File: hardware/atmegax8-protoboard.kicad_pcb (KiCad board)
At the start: 2 copper layers, 22.9 x 55.9 mm, 6 parts, among them IC1 ATMEGA328-P, P1 CONN1, P2 CONN2, P3 SERPROG

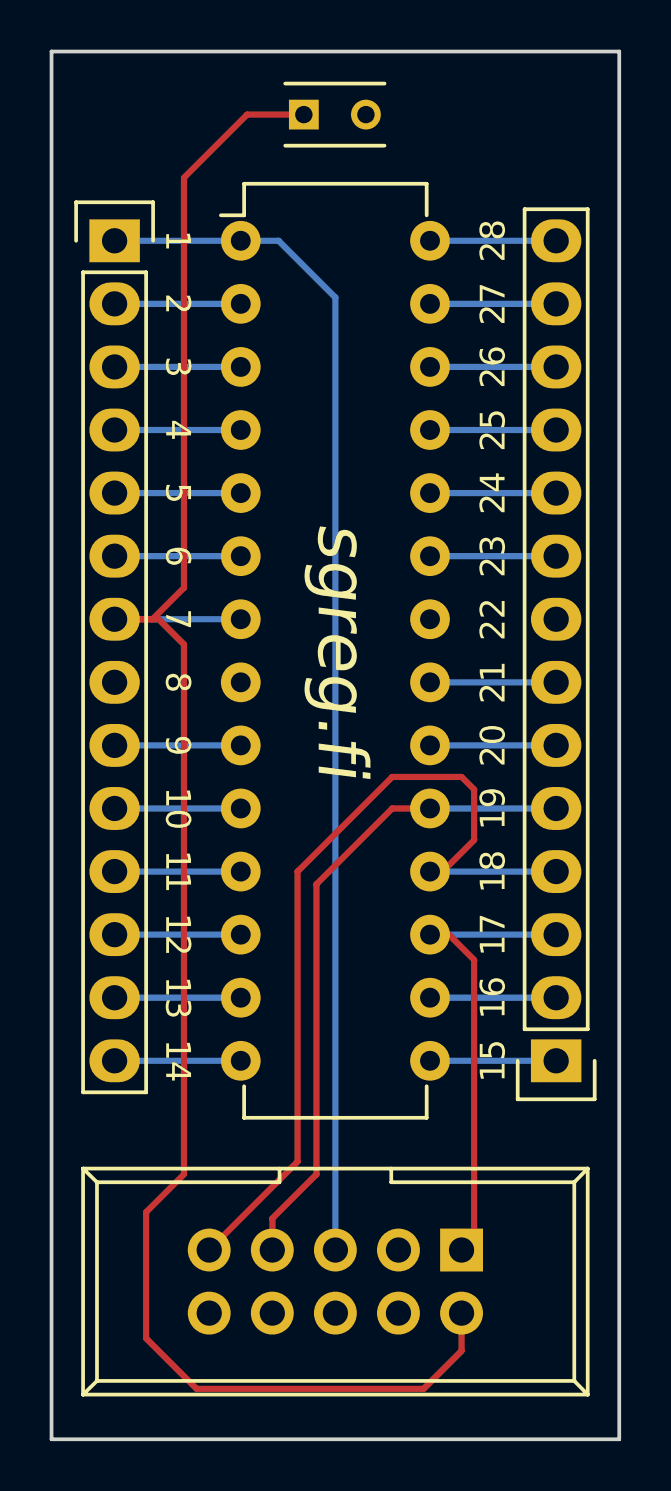
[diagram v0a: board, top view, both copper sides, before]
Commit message: Rev B. PCB, minimized size, re-routed and added jumper
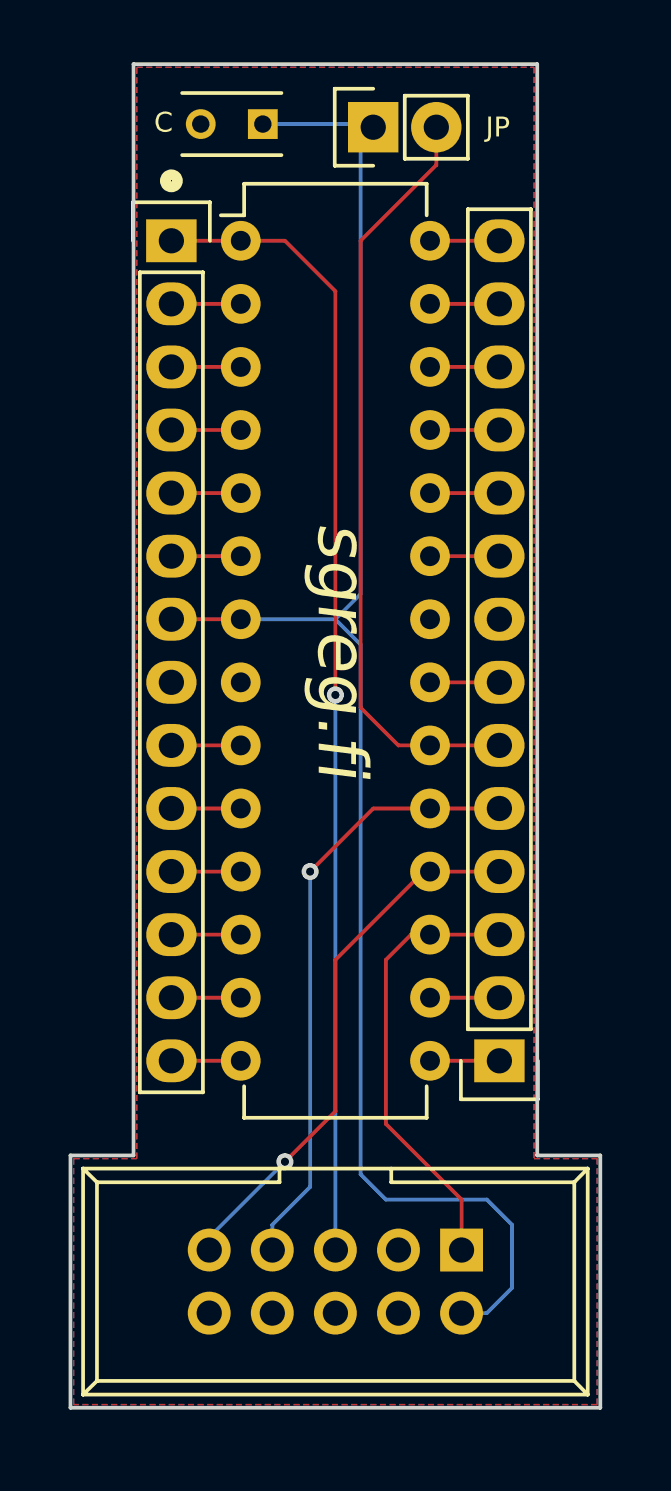
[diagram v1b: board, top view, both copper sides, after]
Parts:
- added JP1: JUMPER, Socket_Strips:Socket_Strip_Straight_1x02, F.Cu at (141.2, 69.1)
- moved P1 2.29 mm to (133.1, 73.7)
- moved P2 2.29 mm to (146.3, 106.7)
- moved C1 1.69 mm to (136.8, 69.0), turned to 180 degrees
- moved G*** 0.13 mm to (139.7, 109.5)
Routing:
- net /AVCC: track 5.08 -> 30.8 mm
- net /VCC: track 79.0 -> 67.0 mm
- net /PB4: track 35.0 -> 23.1 mm, vias 0 -> 1
- net /PD7: track 5.08 -> 2.79 mm
- net /PD6: track 5.08 -> 2.79 mm
- net /PD5: track 5.08 -> 2.79 mm
- net /PD4: track 5.08 -> 2.79 mm
- net /PD3: track 5.08 -> 2.79 mm
- net /PD2: track 5.08 -> 2.79 mm
- net /PD1: track 5.08 -> 2.79 mm
- net /PD0: track 5.08 -> 2.79 mm
- net /PC5: track 5.08 -> 2.79 mm
- net /PC4: track 5.08 -> 2.79 mm
- net /PC3: track 5.08 -> 2.79 mm
- net /PC2: track 5.08 -> 2.79 mm
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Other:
- board size 22.9 x 55.9 mm -> 21.3 x 54.1 mm
- board text added: "05/2016"
- board text added: "C"
- board text added: "JP"
- board text added: "Revision B"
- board text removed: "03/2016"
- board text removed: "1"
- board text removed: "10"
- board text removed: "11"
- board text removed: "12"
- board text removed: "13"
- board text removed: "14"
- board text removed: "15"
- board text removed: "16"
- board text removed: "17"
- board text removed: "18"
- board text removed: "19"
- board text removed: "2"
- board text removed: "20"
- board text removed: "21"
- board text removed: "22"
- board text removed: "23"
- board text removed: "24"
- board text removed: "25"
- board text removed: "26"
- board text removed: "27"
- board text removed: "28"
- board text removed: "3"
- board text removed: "4"
- board text removed: "5"
- board text removed: "6"
- board text removed: "7"
- board text removed: "8"
- board text removed: "9"
- board text removed: "Revision A"
